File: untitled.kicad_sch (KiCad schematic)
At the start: 3 parts

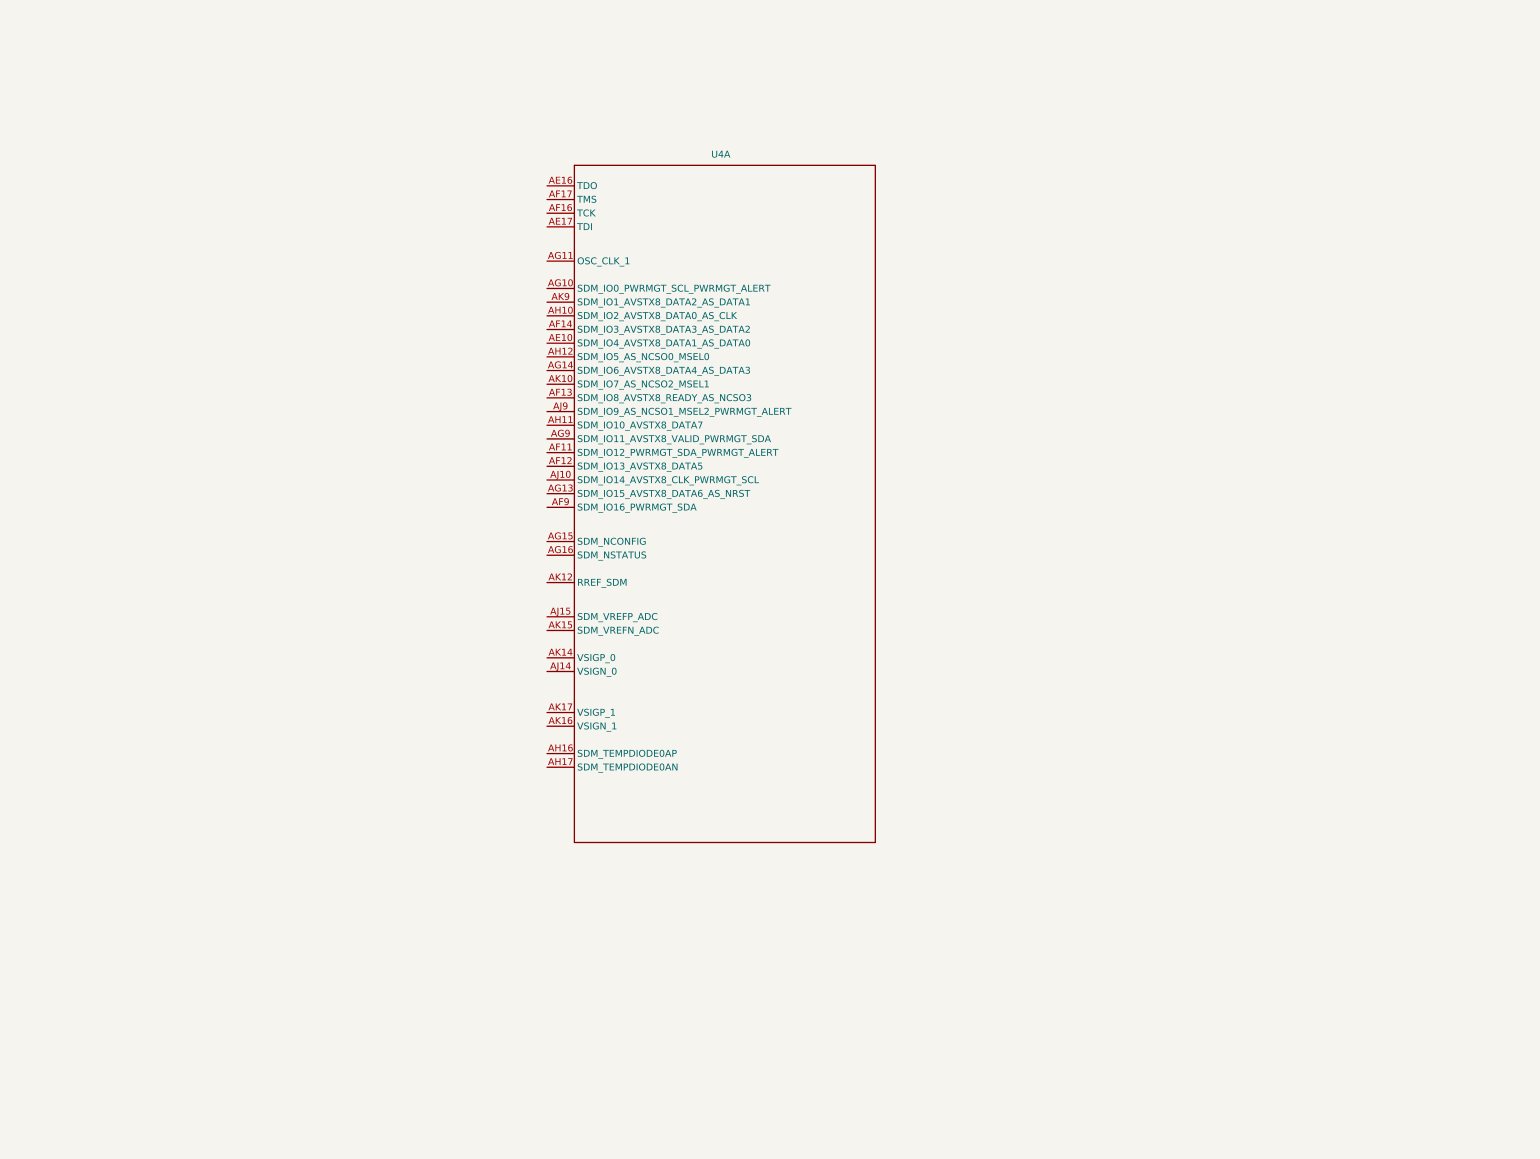
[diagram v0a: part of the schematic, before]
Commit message: move adc and admux to own schematic
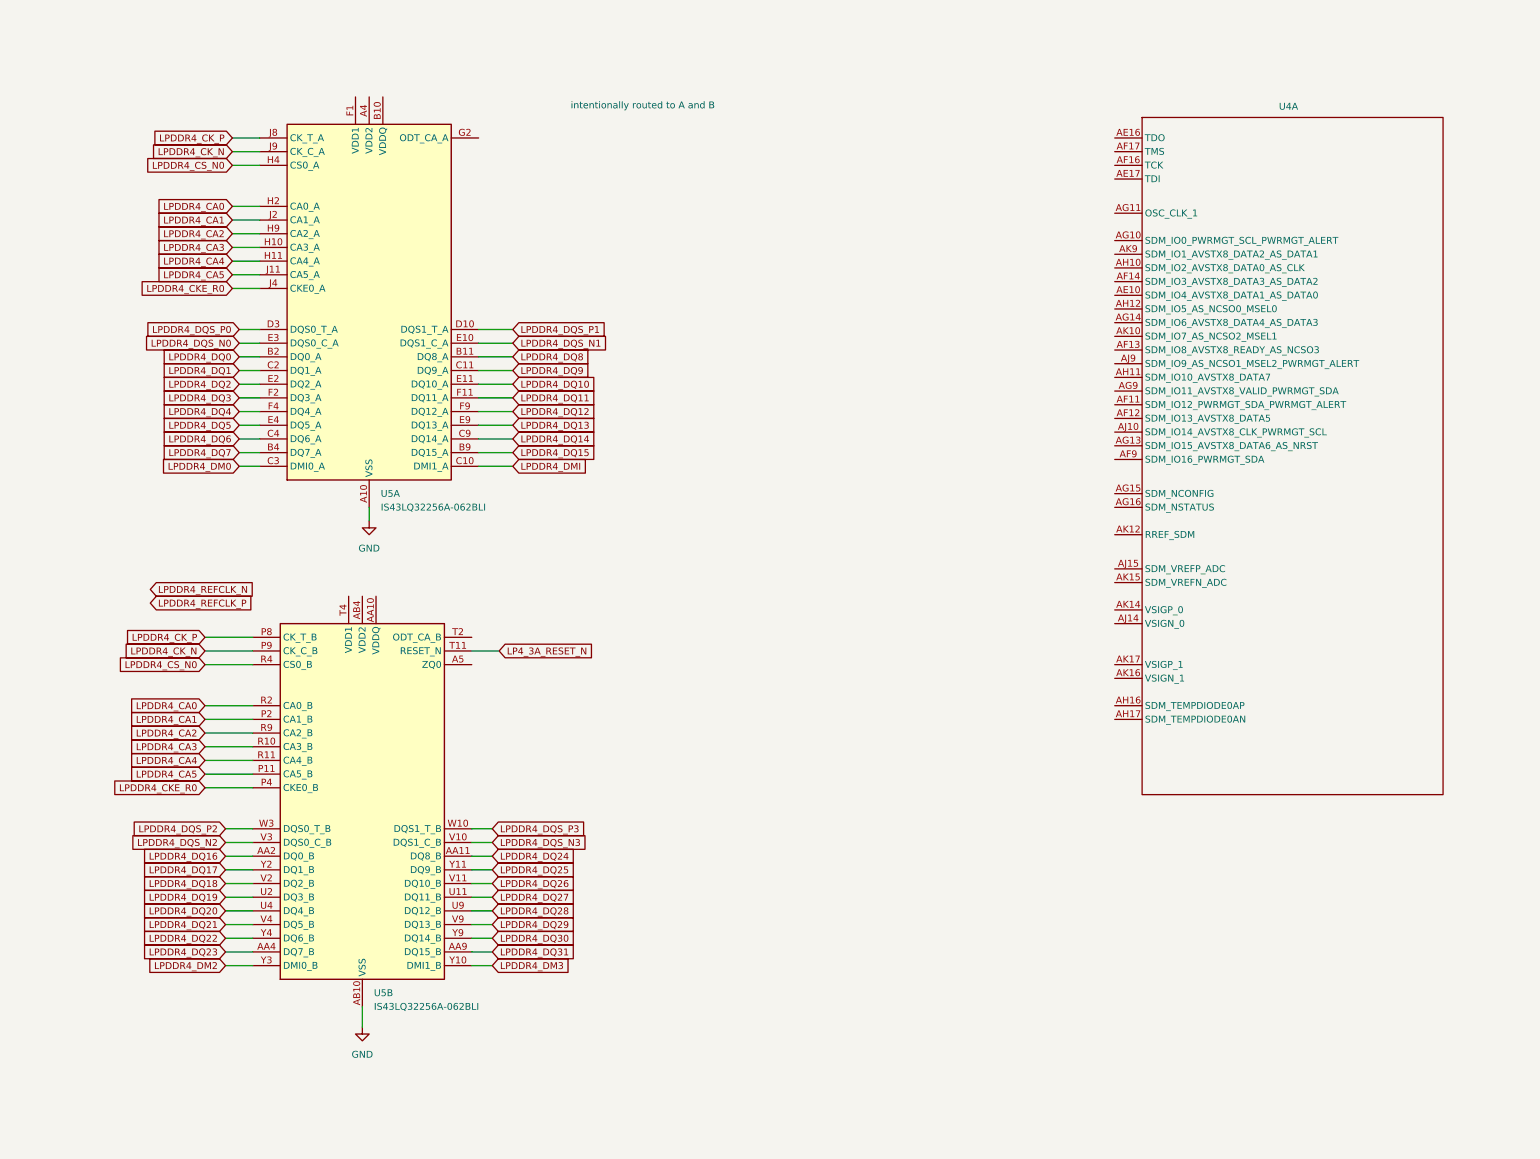
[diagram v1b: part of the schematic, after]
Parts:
- added U5: IS43LQ32256A-062BLI, Package_BGA:BGA-200_10x14.5mm_Layout12x22_P0.8x0.65mm, symbol Memory_RAM:IS43LQ32256A-062BLI
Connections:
- net GND: now also U5.A10 (VSS), U5.A3 (VSS), U5.AB10 (VSS), U5.AB3 (VSS), U5.AB5 (VSS), U5.AB8 (VSS), U5.C1 (VSS), U5.C12 (VSS), U5.C5 (VSS), U5.C8 (VSS), U5.D11 (VSS), U5.D2 (VSS), U5.D4 (VSS), U5.D9 (VSS), U5.E1 (VSS), U5.E12 (VSS), U5.E5 (VSS), U5.E8 (VSS), U5.G1 (VSS), U5.G10 (VSS), U5.G12 (VSS), U5.G3 (VSS), U5.G5 (VSS), U5.G8 (VSS), U5.J1 (VSS), U5.J10 (VSS), U5.J12 (VSS), U5.J3 (VSS), U5.K11 (VSS), U5.K2 (VSS), U5.K4 (VSS), U5.K9 (VSS), U5.N11 (VSS), U5.N2 (VSS), U5.N4 (VSS), U5.N9 (VSS), U5.P1 (VSS), U5.P10 (VSS), U5.P12 (VSS), U5.P3 (VSS), U5.T1 (VSS), U5.T10 (VSS), U5.T12 (VSS), U5.T3 (VSS), U5.T5 (VSS), U5.T8 (VSS), U5.V1 (VSS), U5.V12 (VSS), U5.V5 (VSS), U5.V8 (VSS), U5.W11 (VSS), U5.W2 (VSS), U5.W4 (VSS), U5.W9 (VSS), U5.Y1 (VSS), U5.Y12 (VSS), U5.Y5 (VSS), U5.Y8 (VSS)
- net LP4_3A_RESET_N: now also U5.T11 (RESET_N)
- net LPDDR4_CA0: now also U5.H2 (CA0_A), U5.R2 (CA0_B)
- net LPDDR4_CA1: now also U5.J2 (CA1_A), U5.P2 (CA1_B)
- net LPDDR4_CA2: now also U5.H9 (CA2_A), U5.R9 (CA2_B)
- net LPDDR4_CA3: now also U5.H10 (CA3_A), U5.R10 (CA3_B)
- net LPDDR4_CA4: now also U5.H11 (CA4_A), U5.R11 (CA4_B)
- net LPDDR4_CA5: now also U5.J11 (CA5_A), U5.P11 (CA5_B)
- net LPDDR4_CKE_R0: now also U5.J4 (CKE0_A), U5.P4 (CKE0_B)
- net LPDDR4_CK_N: now also U5.J9 (CK_C_A), U5.P9 (CK_C_B)
- net LPDDR4_CK_P: now also U5.J8 (CK_T_A), U5.P8 (CK_T_B)
- net LPDDR4_CS_N0: now also U5.H4 (CS0_A), U5.R4 (CS0_B)
- net LPDDR4_DM0: now also U5.C3 (DMI0_A)
- net LPDDR4_DM2: now also U5.Y3 (DMI0_B)
- net LPDDR4_DM3: now also U5.Y10 (DMI1_B)
- net LPDDR4_DMI: now also U5.C10 (DMI1_A)
- net LPDDR4_DQ0: now also U5.B2 (DQ0_A)
- net LPDDR4_DQ1: now also U5.C2 (DQ1_A)
- net LPDDR4_DQ10: now also U5.E11 (DQ10_A)
- net LPDDR4_DQ11: now also U5.F11 (DQ11_A)
- net LPDDR4_DQ12: now also U5.F9 (DQ12_A)
- net LPDDR4_DQ13: now also U5.E9 (DQ13_A)
- net LPDDR4_DQ14: now also U5.C9 (DQ14_A)
- net LPDDR4_DQ15: now also U5.B9 (DQ15_A)
- net LPDDR4_DQ16: now also U5.AA2 (DQ0_B)
- net LPDDR4_DQ17: now also U5.Y2 (DQ1_B)
- net LPDDR4_DQ18: now also U5.V2 (DQ2_B)
- net LPDDR4_DQ19: now also U5.U2 (DQ3_B)
- net LPDDR4_DQ2: now also U5.E2 (DQ2_A)
- net LPDDR4_DQ20: now also U5.U4 (DQ4_B)
- net LPDDR4_DQ21: now also U5.V4 (DQ5_B)
- net LPDDR4_DQ22: now also U5.Y4 (DQ6_B)
- net LPDDR4_DQ23: now also U5.AA4 (DQ7_B)
- net LPDDR4_DQ24: now also U5.AA11 (DQ8_B)
- net LPDDR4_DQ25: now also U5.Y11 (DQ9_B)
- net LPDDR4_DQ26: now also U5.V11 (DQ10_B)
- net LPDDR4_DQ27: now also U5.U11 (DQ11_B)
- net LPDDR4_DQ28: now also U5.U9 (DQ12_B)
- net LPDDR4_DQ29: now also U5.V9 (DQ13_B)
- net LPDDR4_DQ3: now also U5.F2 (DQ3_A)
- net LPDDR4_DQ30: now also U5.Y9 (DQ14_B)
- net LPDDR4_DQ31: now also U5.AA9 (DQ15_B)
- net LPDDR4_DQ4: now also U5.F4 (DQ4_A)
- net LPDDR4_DQ5: now also U5.E4 (DQ5_A)
- net LPDDR4_DQ6: now also U5.C4 (DQ6_A)
- net LPDDR4_DQ7: now also U5.B4 (DQ7_A)
- net LPDDR4_DQ8: now also U5.B11 (DQ8_A)
- net LPDDR4_DQ9: now also U5.C11 (DQ9_A)
- net LPDDR4_DQS_N0: now also U5.E3 (DQS0_C_A)
- net LPDDR4_DQS_N1: now also U5.E10 (DQS1_C_A)
- net LPDDR4_DQS_N2: now also U5.V3 (DQS0_C_B)
- net LPDDR4_DQS_N3: now also U5.V10 (DQS1_C_B)
- net LPDDR4_DQS_P0: now also U5.D3 (DQS0_T_A)
- net LPDDR4_DQS_P1: now also U5.D10 (DQS1_T_A)
- net LPDDR4_DQS_P2: now also U5.W3 (DQS0_T_B)
- net LPDDR4_DQS_P3: now also U5.W10 (DQS1_T_B)
- new net: U5.AA10 (VDDQ), U5.AA3 (VDDQ), U5.AA5 (VDDQ), U5.AA8 (VDDQ), U5.U10 (VDDQ), U5.U3 (VDDQ), U5.W1 (VDDQ), U5.W12 (VDDQ), U5.W5 (VDDQ), U5.W8 (VDDQ)
- new net: U5.AB4 (VDD2), U5.AB9 (VDD2), U5.N1 (VDD2), U5.N10 (VDD2), U5.N12 (VDD2), U5.N3 (VDD2), U5.R1 (VDD2), U5.R12 (VDD2), U5.R5 (VDD2), U5.R8 (VDD2), U5.U5 (VDD2), U5.U8 (VDD2)
- new net: U5.T4 (VDD1), U5.T9 (VDD1), U5.U1 (VDD1), U5.U12 (VDD1)
- new net: U5.A4 (VDD2), U5.A9 (VDD2), U5.F5 (VDD2), U5.F8 (VDD2), U5.H1 (VDD2), U5.H12 (VDD2), U5.H5 (VDD2), U5.H8 (VDD2), U5.K1 (VDD2), U5.K10 (VDD2), U5.K12 (VDD2), U5.K3 (VDD2)
- new net: U5.B10 (VDDQ), U5.B3 (VDDQ), U5.B5 (VDDQ), U5.B8 (VDDQ), U5.D1 (VDDQ), U5.D12 (VDDQ), U5.D5 (VDDQ), U5.D8 (VDDQ), U5.F10 (VDDQ), U5.F3 (VDDQ)
- new net: U5.F1 (VDD1), U5.F12 (VDD1), U5.G4 (VDD1), U5.G9 (VDD1)
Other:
- note added: "intentionally routed to A and B"
- moved on the sheet: U4A

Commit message: add vias to lppdr balls
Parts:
- renumbered R2 to R1, R1 to R2, U4 to U1, U5 to U2
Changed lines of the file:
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@@
 		(in_pos_files yes)
 		(dnp no)
-		(property "Reference" "U4"
+		(property "Reference" "U1"
 			(at 240.03 20.828 0)
 			(show_name no)
@@
 			(project "agilex_3_soc"
 				(path "/a5b98d95-6877-4284-904f-d04e32723ae0/e3048211-3a22-4ca2-880d-a02e0bb6b448"
-					(reference "U4")
+					(reference "U1")
 					(unit 1)
 				)
@@
 		(dnp no)
 		(fields_autoplaced yes)
-		(property "Reference" "U4"
+		(property "Reference" "U1"
 			(at 273.05 279.4 0)
 			(show_name no)
@@
 			(project "agilex_3_soc"
 				(path "/a5b98d95-6877-4284-904f-d04e32723ae0/e3048211-3a22-4ca2-880d-a02e0bb6b448"
-					(reference "U4")
+					(reference "U1")
 					(unit 13)
 				)
@@
 		(dnp no)
 		(fields_autoplaced yes)
-		(property "Reference" "U4"
+		(property "Reference" "U1"
 			(at 433.705 33.02 0)
 			(show_name no)
@@
 			(project "agilex_3_soc"
 				(path "/a5b98d95-6877-4284-904f-d04e32723ae0/e3048211-3a22-4ca2-880d-a02e0bb6b448"
-					(reference "U4")
+					(reference "U1")
 					(unit 12)
 				)
@@
 		(dnp no)
 		(fields_autoplaced yes)
-		(property "Reference" "U4"
+		(property "Reference" "U1"
 			(at -60.96 -209.55 0)
 			(show_name no)
@@
 			(project "agilex_3_soc"
 				(path "/a5b98d95-6877-4284-904f-d04e32723ae0/e3048211-3a22-4ca2-880d-a02e0bb6b448"
-					(reference "U4")
+					(reference "U1")
 					(unit 3)
 				)
@@
 		(dnp no)
 		(fields_autoplaced yes)
-		(property "Reference" "#PWR06"
+		(property "Reference" "#PWR015"
 			(at 407.67 210.82 0)
 			(hide yes)
@@
 			(project "agilex_3_soc"
 				(path "/a5b98d95-6877-4284-904f-d04e32723ae0/e3048211-3a22-4ca2-880d-a02e0bb6b448"
-					(reference "#PWR06")
+					(reference "#PWR015")
 					(unit 1)
 				)
@@
 		(dnp no)
 		(fields_autoplaced yes)
-		(property "Reference" "U4"
+		(property "Reference" "U1"
 			(at 544.83 -83.1851 0)
 			(show_name no)
@@
 			(project "agilex_3_soc"
 				(path "/a5b98d95-6877-4284-904f-d04e32723ae0/e3048211-3a22-4ca2-880d-a02e0bb6b448"
-					(reference "U4")
+					(reference "U1")
 					(unit 5)
 				)
@@
 		(dnp no)
 		(fields_autoplaced yes)
-		(property "Reference" "U4"
+		(property "Reference" "U1"
 			(at 424.815 281.94 0)
 			(show_name no)
@@
 			(project "agilex_3_soc"
 				(path "/a5b98d95-6877-4284-904f-d04e32723ae0/e3048211-3a22-4ca2-880d-a02e0bb6b448"
-					(reference "U4")
+					(reference "U1")
 					(unit 7)
 				)
@@
 		(dnp no)
 		(fields_autoplaced yes)
-		(property "Reference" "#PWR09"
+		(property "Reference" "#PWR017"
 			(at 609.6 209.55 0)
 			(hide yes)
@@
 			(project "agilex_3_soc"
 				(path "/a5b98d95-6877-4284-904f-d04e32723ae0/e3048211-3a22-4ca2-880d-a02e0bb6b448"
-					(reference "#PWR09")
+					(reference "#PWR017")
 					(unit 1)
 				)
@@
 		(dnp no)
 		(fields_autoplaced yes)
-		(property "Reference" "#PWR07"
+		(property "Reference" "#PWR016"
 			(at 459.74 208.28 0)
 			(hide yes)
@@
 			(project "agilex_3_soc"
 				(path "/a5b98d95-6877-4284-904f-d04e32723ae0/e3048211-3a22-4ca2-880d-a02e0bb6b448"
-					(reference "#PWR07")
+					(reference "#PWR016")
 					(unit 1)
 				)
@@
 		(dnp no)
 		(fields_autoplaced yes)
-		(property "Reference" "R2"
+		(property "Reference" "R1"
 			(at -153.67 -118.11 90)
 			(show_name no)
@@
 			(project "agilex_3_soc"
 				(path "/a5b98d95-6877-4284-904f-d04e32723ae0/e3048211-3a22-4ca2-880d-a02e0bb6b448"
-					(reference "R2")
+					(reference "R1")
 					(unit 1)
 				)
@@
 		(dnp no)
 		(fields_autoplaced yes)
-		(property "Reference" "#PWR05"
+		(property "Reference" "#PWR013"
 			(at 69.85 198.12 0)
 			(hide yes)
@@
 			(project "agilex_3_soc"
 				(path "/a5b98d95-6877-4284-904f-d04e32723ae0/e3048211-3a22-4ca2-880d-a02e0bb6b448"
-					(reference "#PWR05")
+					(reference "#PWR013")
 					(unit 1)
 				)
@@
 		(dnp no)
 		(fields_autoplaced yes)
-		(property "Reference" "#PWR01"
+		(property "Reference" "#PWR012"
 			(at 58.42 -171.45 0)
 			(hide yes)
@@
 			(project "agilex_3_soc"
 				(path "/a5b98d95-6877-4284-904f-d04e32723ae0/e3048211-3a22-4ca2-880d-a02e0bb6b448"
-					(reference "#PWR01")
+					(reference "#PWR012")
 					(unit 1)
 				)
@@
 		(dnp no)
 		(fields_autoplaced yes)
-		(property "Reference" "U4"
+		(property "Reference" "U1"
 			(at -231.775 5.08 0)
 			(show_name no)
@@
 			(project "agilex_3_soc"
 				(path "/a5b98d95-6877-4284-904f-d04e32723ae0/e3048211-3a22-4ca2-880d-a02e0bb6b448"
-					(reference "U4")
+					(reference "U1")
 					(unit 10)
 				)
@@
 		(dnp no)
 		(fields_autoplaced yes)
-		(property "Reference" "U5"
+		(property "Reference" "U2"
 			(at 71.9933 185.42 0)
 			(show_name no)
@@
 			(project "agilex_3_soc"
 				(path "/a5b98d95-6877-4284-904f-d04e32723ae0/e3048211-3a22-4ca2-880d-a02e0bb6b448"
-					(reference "U5")
+					(reference "U2")
 					(unit 2)
 				)
@@
 		(dnp no)
 		(fields_autoplaced yes)
-		(property "Reference" "#PWR04"
+		(property "Reference" "#PWR014"
 			(at 71.12 104.14 0)
 			(hide yes)
@@
 			(project "agilex_3_soc"
 				(path "/a5b98d95-6877-4284-904f-d04e32723ae0/e3048211-3a22-4ca2-880d-a02e0bb6b448"
-					(reference "#PWR04")
+					(reference "#PWR014")
 					(unit 1)
 				)
@@
 		(dnp no)
 		(fields_autoplaced yes)
-		(property "Reference" "U4"
+		(property "Reference" "U1"
 			(at 76.835 283.21 0)
 			(show_name no)
@@
 			(project "agilex_3_soc"
 				(path "/a5b98d95-6877-4284-904f-d04e32723ae0/e3048211-3a22-4ca2-880d-a02e0bb6b448"
-					(reference "U4")
+					(reference "U1")
 					(unit 8)
 				)
@@
 		(dnp no)
 		(fields_autoplaced yes)
-		(property "Reference" "U4"
+		(property "Reference" "U1"
 			(at -245.11 -203.2 0)
 			(show_name no)
@@
 			(project "agilex_3_soc"
 				(path "/a5b98d95-6877-4284-904f-d04e32723ae0/e3048211-3a22-4ca2-880d-a02e0bb6b448"
-					(reference "U4")
+					(reference "U1")
 					(unit 2)
 				)
@@
 		(dnp no)
 		(fields_autoplaced yes)
-		(property "Reference" "R1"
+		(property "Reference" "R2"
 			(at 49.53 -185.42 90)
 			(show_name no)
@@
 			(project "agilex_3_soc"
 				(path "/a5b98d95-6877-4284-904f-d04e32723ae0/e3048211-3a22-4ca2-880d-a02e0bb6b448"
-					(reference "R1")
+					(reference "R2")
 					(unit 1)
 				)
@@
 		(dnp no)
 		(fields_autoplaced yes)
-		(property "Reference" "U4"
+		(property "Reference" "U1"
 			(at 183.515 -167.64 0)
 			(show_name no)
@@
 			(project "agilex_3_soc"
 				(path "/a5b98d95-6877-4284-904f-d04e32723ae0/e3048211-3a22-4ca2-880d-a02e0bb6b448"
-					(reference "U4")
+					(reference "U1")
 					(unit 4)
 				)
@@
 		(dnp no)
 		(fields_autoplaced yes)
-		(property "Reference" "#PWR02"
+		(property "Reference" "#PWR011"
 			(at -165.1 -104.14 0)
 			(hide yes)
@@
 			(project "agilex_3_soc"
 				(path "/a5b98d95-6877-4284-904f-d04e32723ae0/e3048211-3a22-4ca2-880d-a02e0bb6b448"
-					(reference "#PWR02")
+					(reference "#PWR011")
 					(unit 1)
 				)
@@
 		(dnp no)
 		(fields_autoplaced yes)
-		(property "Reference" "#PWR08"
+		(property "Reference" "#PWR018"
 			(at 647.7 208.28 0)
 			(hide yes)
@@
 			(project "agilex_3_soc"
 				(path "/a5b98d95-6877-4284-904f-d04e32723ae0/e3048211-3a22-4ca2-880d-a02e0bb6b448"
-					(reference "#PWR08")
+					(reference "#PWR018")
 					(unit 1)
 				)
@@
 		(dnp no)
 		(fields_autoplaced yes)
-		(property "Reference" "U4"
+		(property "Reference" "U1"
 			(at 713.74 -49.53 0)
 			(show_name no)
@@
 			(project "agilex_3_soc"
 				(path "/a5b98d95-6877-4284-904f-d04e32723ae0/e3048211-3a22-4ca2-880d-a02e0bb6b448"
-					(reference "U4")
+					(reference "U1")
 					(unit 6)
 				)
@@
 		(dnp no)
 		(fields_autoplaced yes)
-		(property "Reference" "U4"
+		(property "Reference" "U1"
 			(at 628.65 34.29 0)
 			(show_name no)
@@
 			(project "agilex_3_soc"
 				(path "/a5b98d95-6877-4284-904f-d04e32723ae0/e3048211-3a22-4ca2-880d-a02e0bb6b448"
-					(reference "U4")
+					(reference "U1")
 					(unit 11)
 				)
@@
 		(dnp no)
 		(fields_autoplaced yes)
-		(property "Reference" "U5"
+		(property "Reference" "U2"
 			(at 73.2633 92.71 0)
 			(show_name no)
@@
 			(project "agilex_3_soc"
 				(path "/a5b98d95-6877-4284-904f-d04e32723ae0/e3048211-3a22-4ca2-880d-a02e0bb6b448"
-					(reference "U5")
+					(reference "U2")
 					(unit 1)
 				)
@@
 		(dnp no)
 		(fields_autoplaced yes)
-		(property "Reference" "U4"
+		(property "Reference" "U1"
 			(at -205.74 222.25 0)
 			(show_name no)
@@
 			(project "agilex_3_soc"
 				(path "/a5b98d95-6877-4284-904f-d04e32723ae0/e3048211-3a22-4ca2-880d-a02e0bb6b448"
-					(reference "U4")
+					(reference "U1")
 					(unit 9)
 				)
